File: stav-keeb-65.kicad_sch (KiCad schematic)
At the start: 56 parts, among them U1 RP2040, U7 W25Q128JVSIQTR, U8 RT9013-33GB, U9 OPA320AIDBVR, X1 X322512MSB4SI

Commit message: Review fixes
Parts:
- C113, C114: value 20pF -> 33pF; LCSC Part C1648 -> C1663
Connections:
- net +3V3: now also C115.2, C135.2, U7.8 (VCC); no longer C115.1, C135.1
- net GND: now also C115.1, C135.1
- net +2V5_RREF renamed +2V5_REF
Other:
- note added: "DO NOT POUR COPPER"
- note removed: "DO NOT POOR COPPER"
- moved on the sheet: C116, C117, C118, C119, C120, C121, C122, D1, D2, F1, FB1, R103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

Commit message: initial pcb and layout.json
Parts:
- F1: footprint (none) -> Fuse:Fuse_1812_4532Metric_Pad1.30x3.40mm_HandSolder
- FB1: footprint (none) -> Inductor_SMD:L_0805_2012Metric_Pad1.05x1.20mm_HandSolder
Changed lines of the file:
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@@
 			)
 		)
-		(property "Footprint" ""
+		(property "Footprint" "Fuse:Fuse_1812_4532Metric_Pad1.30x3.40mm_HandSolder"
 			(at 247.65 25.908 90)
 			(hide yes)
@@
 			)
 		)
-		(property "Footprint" ""
+		(property "Footprint" "Inductor_SMD:L_0805_2012Metric_Pad1.05x1.20mm_HandSolder"
 			(at 274.32 20.828 90)
 			(hide yes)

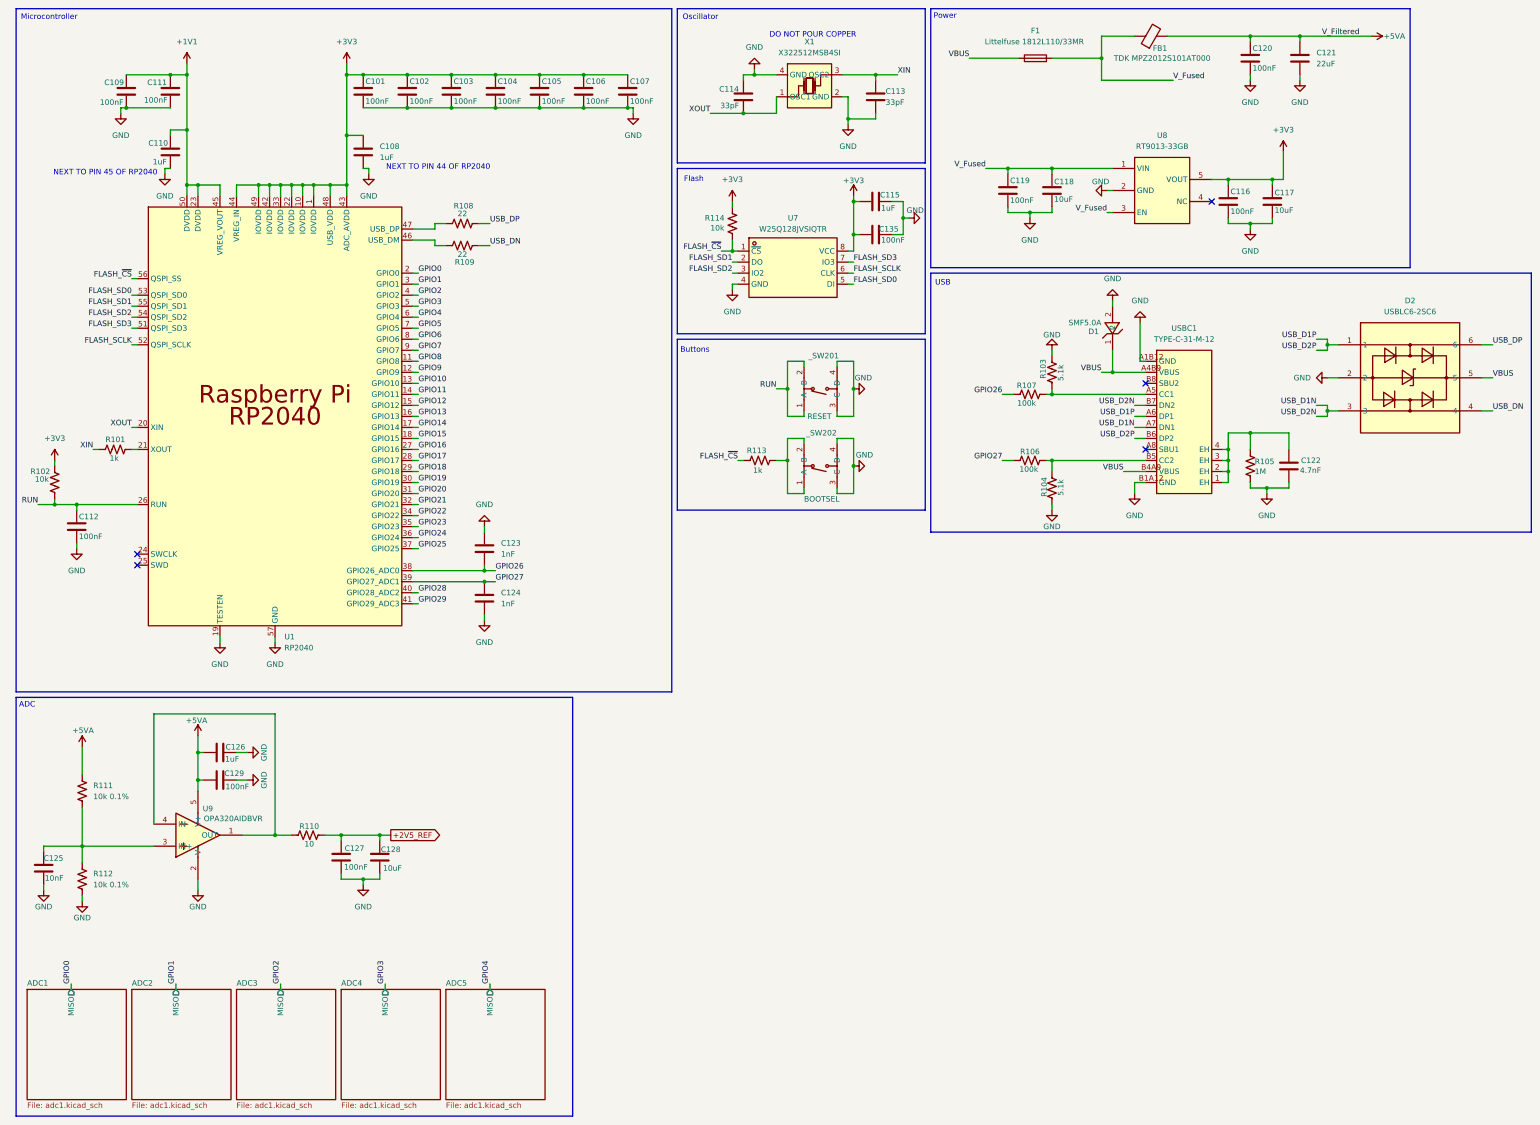
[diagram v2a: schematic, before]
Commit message: initial script for sensor placement, and schematic fixes
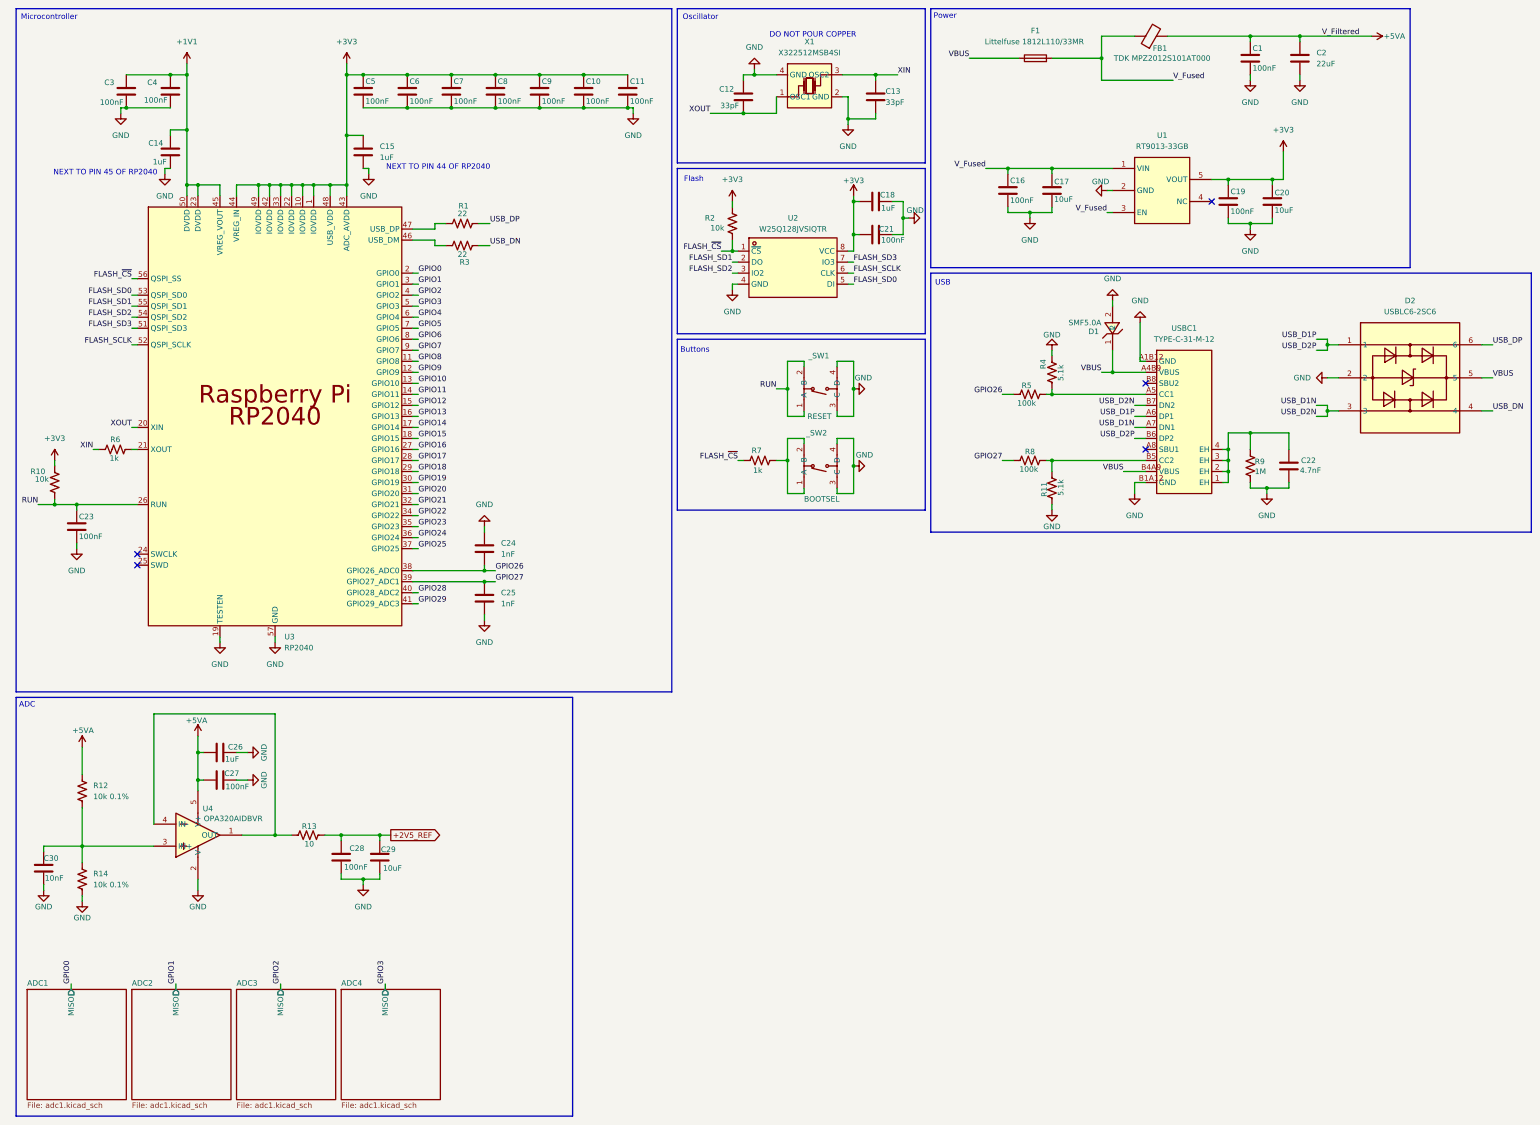
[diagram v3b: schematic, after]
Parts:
- renumbered C120 to C1, C106 to C10, C107 to C11, C114 to C12, C113 to C13, C110 to C14, C108 to C15, C119 to C16, C118 to C17, C115 to C18, C116 to C19, C121 to C2, C117 to C20, C135 to C21, C122 to C22, C112 to C23, C123 to C24, C124 to C25, C126 to C26, C129 to C27, C127 to C28, C128 to C29, C109 to C3, C125 to C30, C111 to C4, C101 to C5, C102 to C6, C103 to C7, C104 to C8, C105 to C9, R108 to R1, R102 to R10, R104 to R11, R111 to R12, R110 to R13, R112 to R14, R114 to R2, R109 to R3, R103 to R4, R107 to R5, R101 to R6, R113 to R7, R106 to R8, R105 to R9, U8 to U1, U7 to U2, U1 to U3, U9 to U4, _SW201 to _SW1, _SW202 to _SW2
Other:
- removed sheet ADC5

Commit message: PCB layout v1
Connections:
- net XIN: now also U3.20 (XIN); no longer R6.1
- net XOUT: now also R6.1; no longer U3.20 (XIN)
- net RP_USB_DN: now reaches R3.2, U3.46 (USB_DM)
- net RP_USB_DP: now reaches R1.2, U3.47 (USB_DP)
- net GPIO0 renamed ADC_MISO
- net GPIO1: no longer names the net of U3.3 (GPIO1)
- net GPIO10: no longer names the net of U3.13 (GPIO10)
- net GPIO11: no longer names the net of U3.14 (GPIO11)
- net GPIO12: no longer names the net of U3.15 (GPIO12)
- net GPIO13: no longer names the net of U3.16 (GPIO13)
- net GPIO14: no longer names the net of U3.17 (GPIO14)
- net GPIO15: no longer names the net of U3.18 (GPIO15)
- net GPIO16: no longer names the net of U3.27 (GPIO16)
- net GPIO17: no longer names the net of U3.28 (GPIO17)
- net GPIO18: no longer names the net of U3.29 (GPIO18)
- net GPIO19: no longer names the net of U3.30 (GPIO19)
- net GPIO2 renamed ADC_SCK
- net GPIO20: no longer names the net of U3.31 (GPIO20)
- net GPIO21: no longer names the net of U3.32 (GPIO21)
- net GPIO22: no longer names the net of U3.34 (GPIO22)
- net GPIO23: no longer names the net of U3.35 (GPIO23)
- net GPIO24: no longer names the net of U3.36 (GPIO24)
- net GPIO25: no longer names the net of U3.37 (GPIO25)
- net GPIO28: no longer names the net of U3.40 (GPIO28_ADC2)
- net GPIO29: no longer names the net of U3.41 (GPIO29_ADC3)
- net GPIO3 renamed ADC_MOSI
- net GPIO4 renamed ADC_~{CS}1
- net GPIO5 renamed ADC_~{CS}2
- net GPIO6 renamed ADC_~{CS}3
- net GPIO7 renamed ADC_~{CS}4
- net GPIO8: no longer names the net of U3.11 (GPIO8)
- net GPIO9: no longer names the net of U3.12 (GPIO9)
- no-connect marks 5 -> 26
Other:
- sheet ADC1 ports: added ~{CS}; removed MISO
- sheet ADC2 ports: added ~{CS}; removed MISO
- sheet ADC3 ports: added ~{CS}; removed MISO
- sheet ADC4 ports: added ~{CS}; removed MISO
- moved on the sheet: R1, R3

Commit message: progress towards v2
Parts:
- added R33, R38, R39, R40, R41, R42, R43, R44, R45, R46, R47, R48: 33, Resistor_SMD:R_0402_1005Metric, symbol Device:R_US
- R1, R10, R11, R13, R2, R3, R4, R5, R6, R7, R8, R9: footprint Resistor_SMD:R_0603_1608Metric_Pad0.98x0.95mm_HandSolder -> Resistor_SMD:R_0402_1005Metric
- R12, R14: footprint Resistor_SMD:R_0603_1608Metric_Pad0.98x0.95mm_HandSolder -> Resistor_SMD:R_0603_1608Metric
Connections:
- net ADC_MISO0: now reaches U3.13 (GPIO10)
- net ADC_MISO1: now reaches U3.14 (GPIO11)
- net ADC_MISO2: now reaches U3.15 (GPIO12)
- net ADC_MISO3: now reaches U3.16 (GPIO13)
- net RP2040_MOSI: now reaches U3.17 (GPIO14)
- net RP2040_MOSI: now also R33.1, R38.1, R39.1, R40.1
- net RP2040_SCK: now reaches U3.18 (GPIO15)
- net RP2040_SCK: now also R41.1, R42.1, R43.1, R44.1
- net RP2040_CS_N: now reaches U3.27 (GPIO16)
- net RP2040_CS_N: now also R45.1, R46.1, R47.1, R48.1
- net ADC_MISO: no longer names the net of U3.2 (GPIO0)
- net ADC_MOSI: no longer names the net of U3.5 (GPIO3)
- net ADC_SCK: no longer names the net of U3.4 (GPIO2)
- net ADC_~{CS}1: no longer names the net of U3.6 (GPIO4)
- net ADC_~{CS}2: no longer names the net of U3.7 (GPIO5)
- net ADC_~{CS}3: no longer names the net of U3.8 (GPIO6)
- net ADC_~{CS}4: no longer names the net of U3.9 (GPIO7)
- new net ADC_MOSI0: R38.2
- new net ADC_MOSI1: R33.2
- new net ADC_MOSI2: R39.2
- new net ADC_MOSI3: R40.2
- new net ADC_SCK0: R41.2
- new net ADC_SCK1: R42.2
- new net ADC_SCK2: R43.2
- new net ADC_SCK3: R44.2
- new net ADC_SC_N0: R45.2
- new net ADC_SC_N1: R46.2
- new net ADC_SC_N2: R47.2
- new net ADC_SC_N3: R48.2
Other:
- sheet ADC1 ports: added CS_N, MISO, MOSI, SCLK; removed ~{CS}
- sheet ADC2 ports: added CS_N, MISO, MOSI, SCLK; removed ~{CS}
- sheet ADC3 ports: added CS_N, MISO, MOSI, SCLK; removed ~{CS}
- sheet ADC4 ports: added CS_N, MISO, MOSI, SCLK; removed ~{CS}

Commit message: more progress towards v2
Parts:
- C1, C16, C19: footprint Capacitor_SMD:C_0603_1608Metric_Pad1.08x0.95mm_HandSolder -> Capacitor_SMD:C_1206_3216Metric
- C10, C11, C12, C13, C14, C15, C18, C21, C22, C23, C24, C25, C26, C27, C28, C3, C30, C4, C5, C6, C7, C8, C9: footprint Capacitor_SMD:C_0603_1608Metric_Pad1.08x0.95mm_HandSolder -> Capacitor_SMD:C_0402_1005Metric
- C17, C2, C20: footprint Capacitor_SMD:C_1206_3216Metric_Pad1.33x1.80mm_HandSolder -> Capacitor_SMD:C_1206_3216Metric
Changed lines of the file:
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@@
 			)
 		)
-		(property "Footprint" "Capacitor_SMD:C_0603_1608Metric_Pad1.08x0.95mm_HandSolder"
+		(property "Footprint" "Capacitor_SMD:C_0402_1005Metric"
 			(at 49.2252 49.53 0)
 			(hide yes)
@@
 			)
 		)
-		(property "Footprint" "Capacitor_SMD:C_1206_3216Metric_Pad1.33x1.80mm_HandSolder"
+		(property "Footprint" "Capacitor_SMD:C_1206_3216Metric"
 			(at 303.2252 60.96 0)
 			(hide yes)
@@
 			)
 		)
-		(property "Footprint" "Capacitor_SMD:C_0603_1608Metric_Pad1.08x0.95mm_HandSolder"
+		(property "Footprint" "Capacitor_SMD:C_0402_1005Metric"
 			(at 124.1552 35.56 0)
 			(hide yes)
@@
 			)
 		)
-		(property "Footprint" "Capacitor_SMD:C_0603_1608Metric_Pad1.08x0.95mm_HandSolder"
+		(property "Footprint" "Capacitor_SMD:C_0402_1005Metric"
 			(at 63.5 183.1848 0)
 			(hide yes)
@@
 			)
 		)
-		(property "Footprint" "Capacitor_SMD:C_0603_1608Metric_Pad1.08x0.95mm_HandSolder"
+		(property "Footprint" "Capacitor_SMD:C_0402_1005Metric"
 			(at 93.6752 49.53 0)
 			(hide yes)
@@
 			)
 		)
-		(property "Footprint" "Capacitor_SMD:C_0603_1608Metric_Pad1.08x0.95mm_HandSolder"
+		(property "Footprint" "Capacitor_SMD:C_0402_1005Metric"
 			(at 181.3052 36.83 0)
 			(hide yes)
@@
 			)
 		)
-		(property "Footprint" "Capacitor_SMD:C_0603_1608Metric_Pad1.08x0.95mm_HandSolder"
+		(property "Footprint" "Capacitor_SMD:C_0402_1005Metric"
 			(at 121.6152 140.97 0)
 			(hide yes)
@@
 			)
 		)
-		(property "Footprint" "Capacitor_SMD:C_0603_1608Metric_Pad1.08x0.95mm_HandSolder"
+		(property "Footprint" "Capacitor_SMD:C_0402_1005Metric"
 			(at 93.6752 35.56 0)
 			(hide yes)
@@
 			)
 		)
-		(property "Footprint" "Capacitor_SMD:C_1206_3216Metric_Pad1.33x1.80mm_HandSolder"
+		(property "Footprint" "Capacitor_SMD:C_1206_3216Metric"
 			(at 309.5752 27.94 0)
 			(hide yes)
@@
 			)
 		)
-		(property "Footprint" "Capacitor_SMD:C_0603_1608Metric_Pad1.08x0.95mm_HandSolder"
+		(property "Footprint" "Capacitor_SMD:C_0402_1005Metric"
 			(at 211.7852 36.83 0)
 			(hide yes)
@@
 			)
 		)
-		(property "Footprint" "Capacitor_SMD:C_1206_3216Metric_Pad1.33x1.80mm_HandSolder"
+		(property "Footprint" "Capacitor_SMD:C_1206_3216Metric"
 			(at 252.4252 58.42 0)
 			(hide yes)
@@
 			)
 		)
-		(property "Footprint" "Capacitor_SMD:C_0603_1608Metric_Pad1.08x0.95mm_HandSolder"
+		(property "Footprint" "Capacitor_SMD:C_0402_1005Metric"
 			(at 86.6648 204.47 0)
 			(hide yes)
@@
 			)
 		)
-		(property "Footprint" "Capacitor_SMD:C_0603_1608Metric_Pad1.08x0.95mm_HandSolder"
+		(property "Footprint" "Capacitor_SMD:C_0402_1005Metric"
 			(at 113.9952 35.56 0)
 			(hide yes)
@@
 			)
 		)
-		(property "Footprint" "Capacitor_SMD:C_0603_1608Metric_Pad1.08x0.95mm_HandSolder"
+		(property "Footprint" "Capacitor_SMD:C_0402_1005Metric"
 			(at 134.3152 35.56 0)
 			(hide yes)
@@
 			)
 		)
-		(property "Footprint" "Capacitor_SMD:C_0603_1608Metric_Pad1.08x0.95mm_HandSolder"
+		(property "Footprint" "Capacitor_SMD:C_0402_1005Metric"
 			(at 307.0352 121.92 0)
 			(hide yes)
@@
 			)
 		)
-		(property "Footprint" "Capacitor_SMD:C_0603_1608Metric_Pad1.08x0.95mm_HandSolder"
+		(property "Footprint" "Capacitor_SMD:C_1206_3216Metric"
 			(at 293.0652 60.96 0)
 			(hide yes)
@@
 			)
 		)
-		(property "Footprint" "Capacitor_SMD:C_0603_1608Metric_Pad1.08x0.95mm_HandSolder"
+		(property "Footprint" "Capacitor_SMD:C_0402_1005Metric"
 			(at 154.6352 35.56 0)
 			(hide yes)
@@
 			)
 		)
-		(property "Footprint" "Capacitor_SMD:C_0603_1608Metric_Pad1.08x0.95mm_HandSolder"
+		(property "Footprint" "Capacitor_SMD:C_0402_1005Metric"
 			(at 207.01 65.7352 0)
 			(hide yes)
@@
 			)
 		)
-		(property "Footprint" "Capacitor_SMD:C_0603_1608Metric_Pad1.08x0.95mm_HandSolder"
+		(property "Footprint" "Capacitor_SMD:C_0402_1005Metric"
 			(at 27.6352 135.89 0)
 			(hide yes)
@@
 			)
 		)
-		(property "Footprint" "Capacitor_SMD:C_0603_1608Metric_Pad1.08x0.95mm_HandSolder"
+		(property "Footprint" "Capacitor_SMD:C_0402_1005Metric"
 			(at 144.4752 35.56 0)
 			(hide yes)
@@
 			)
 		)
-		(property "Footprint" "Capacitor_SMD:C_0603_1608Metric_Pad1.08x0.95mm_HandSolder"
+		(property "Footprint" "Capacitor_SMD:C_0402_1005Metric"
 			(at 39.0652 35.56 0)
 			(hide yes)
@@
 			)
 		)
-		(property "Footprint" "Capacitor_SMD:C_0603_1608Metric_Pad1.08x0.95mm_HandSolder"
+		(property "Footprint" "Capacitor_SMD:C_1206_3216Metric"
 			(at 298.1452 27.94 0)
 			(hide yes)
@@
 			)
 		)
-		(property "Footprint" "Capacitor_SMD:C_0603_1608Metric_Pad1.08x0.95mm_HandSolder"
+		(property "Footprint" "Capacitor_SMD:C_0402_1005Metric"
 			(at 55.88 191.4652 0)
 			(hide yes)
@@
 			)
 		)
-		(property "Footprint" "Capacitor_SMD:C_0603_1608Metric_Pad1.08x0.95mm_HandSolder"
+		(property "Footprint" "Capacitor_SMD:C_0402_1005Metric"
 			(at 49.2252 35.56 0)
 			(hide yes)
@@
 			)
 		)
-		(property "Footprint" "Capacitor_SMD:C_0603_1608Metric_Pad1.08x0.95mm_HandSolder"
+		(property "Footprint" "Capacitor_SMD:C_0402_1005Metric"
 			(at 103.8352 35.56 0)
 			(hide yes)
@@
 			)
 		)
-		(property "Footprint" "Capacitor_SMD:C_0603_1608Metric_Pad1.08x0.95mm_HandSolder"
+		(property "Footprint" "Capacitor_SMD:C_0402_1005Metric"
 			(at 207.01 58.1152 0)
 			(hide yes)
@@
 			)
 		)
-		(property "Footprint" "Capacitor_SMD:C_0603_1608Metric_Pad1.08x0.95mm_HandSolder"
+		(property "Footprint" "Capacitor_SMD:C_1206_3216Metric"
 			(at 242.2652 58.42 0)
 			(hide yes)
@@
 			)
 		)
-		(property "Footprint" "Capacitor_SMD:C_0603_1608Metric_Pad1.08x0.95mm_HandSolder"
+		(property "Footprint" "Capacitor_SMD:C_0402_1005Metric"
 			(at 20.0152 214.63 0)
 			(hide yes)
@@
 			)
 		)
-		(property "Footprint" "Capacitor_SMD:C_0603_1608Metric_Pad1.08x0.95mm_HandSolder"
+		(property "Footprint" "Capacitor_SMD:C_0402_1005Metric"
 			(at 121.6152 152.4 0)
 			(hide yes)

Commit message: closer to v2
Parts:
- C22: footprint Capacitor_SMD:C_0402_1005Metric -> Capacitor_SMD:C_1206_3216Metric
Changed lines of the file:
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@@
 			)
 		)
-		(property "Footprint" "Capacitor_SMD:C_0402_1005Metric"
+		(property "Footprint" "Capacitor_SMD:C_1206_3216Metric"
 			(at 307.0352 121.92 0)
 			(hide yes)
